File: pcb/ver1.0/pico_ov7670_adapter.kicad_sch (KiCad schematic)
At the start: 22 parts, among them J1 GPIO Header, SW1 SW_Push, SW2 SW_Push, U1 CAMERA-OV7670, U2 RASPBERRY_PI_PICO_W

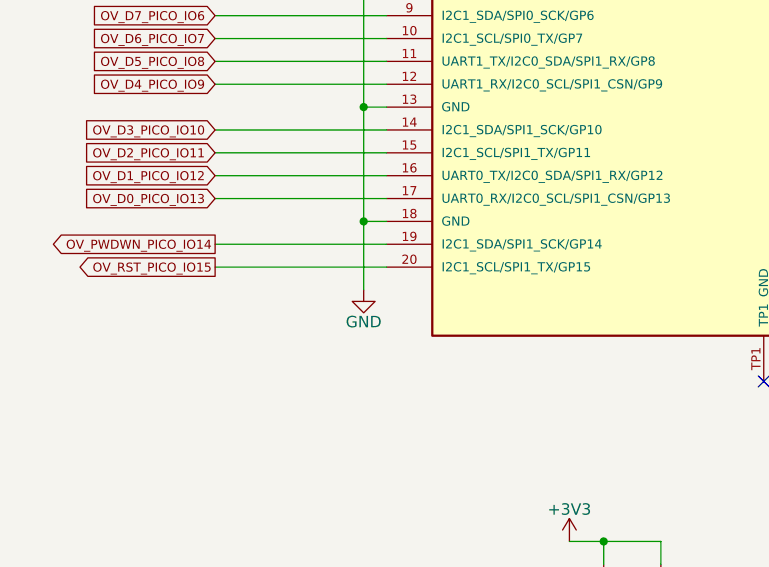
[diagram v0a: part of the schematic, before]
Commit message: camera module footptint updated.
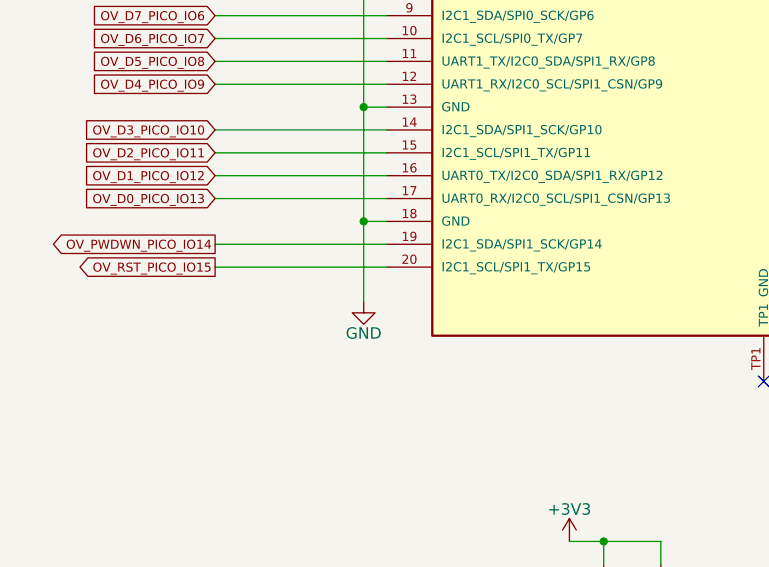
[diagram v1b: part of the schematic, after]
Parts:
- U1: footprint pico_ov7670_adapter:ov7670_camera module -> pico_ov7670_adapter:CAMERA-OV7670-DIP
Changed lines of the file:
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@@
 	)
 	(junction
-		(at 71.12 86.36)
-		(diameter 0)
-		(color 0 0 0 0)
-	)
-	(junction
 		(at 240.03 114.3)
 		(diameter 0)
@@
 		(color 0 0 0 0)
 	)
+	(junction
+		(at 71.12 86.36)
+		(diameter 0)
+		(color 0 0 0 0)
+	)
 	(no_connect
 		(at 170.18 55.88)
@@
 	(wire
 		(pts
+			(xy 71.12 86.36) (xy 71.12 95.25)
+		)
+		(stroke
+			(width 0)
+			(type default)
+		)
+	)
+	(wire
+		(pts
 			(xy 248.92 35.56) (xy 257.81 35.56)
 		)
@@
 	(wire
 		(pts
-			(xy 71.12 86.36) (xy 71.12 93.98)
-		)
-		(stroke
-			(width 0)
-			(type default)
-		)
-	)
-	(wire
-		(pts
 			(xy 240.03 104.14) (xy 240.03 106.68)
 		)
@@
 			)
 		)
-		(property "Footprint" "pico_ov7670_adapter:ov7670_camera module"
+		(property "Footprint" "pico_ov7670_adapter:CAMERA-OV7670-DIP"
 			(at 121.92 147.32 0)
 			(effects
@@
 	(symbol
 		(lib_id "power:GND")
-		(at 71.12 93.98 0)
+		(at 71.12 95.25 0)
 		(unit 1)
 		(exclude_from_sim no)
@@
 		(dnp no)
 		(property "Reference" "#PWR01"
-			(at 71.12 100.33 0)
+			(at 71.12 101.6 0)
 			(effects
 				(font
@@
 		)
 		(property "Value" "GND"
-			(at 71.12 97.536 0)
+			(at 71.12 98.806 0)
 			(effects
 				(font
@@
 		)
 		(property "Footprint" ""
-			(at 71.12 93.98 0)
+			(at 71.12 95.25 0)
 			(effects
 				(font
@@
 		)
 		(property "Datasheet" ""
-			(at 71.12 93.98 0)
+			(at 71.12 95.25 0)
 			(effects
 				(font
@@
 		)
 		(property "Description" "Power symbol creates a global label with name \"GND\" , ground"
-			(at 71.12 93.98 0)
+			(at 71.12 95.25 0)
 			(effects
 				(font
@@
 		)
 		(instances
-			(project ""
+			(project "pico_ov7670_adapter"
 				(path "/8ca4dbff-a6fb-40ff-ba8a-6032e61c2093"
 					(reference "#PWR01")
